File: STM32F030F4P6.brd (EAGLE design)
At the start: 19.1 x 50.8 mm, 27 parts, among them IC1 MCP170333MB, J2 455-1750-1-ND, J4 CORTEX_DEBUG_MINIMUM_PTH, U1 STM32F030F4P6

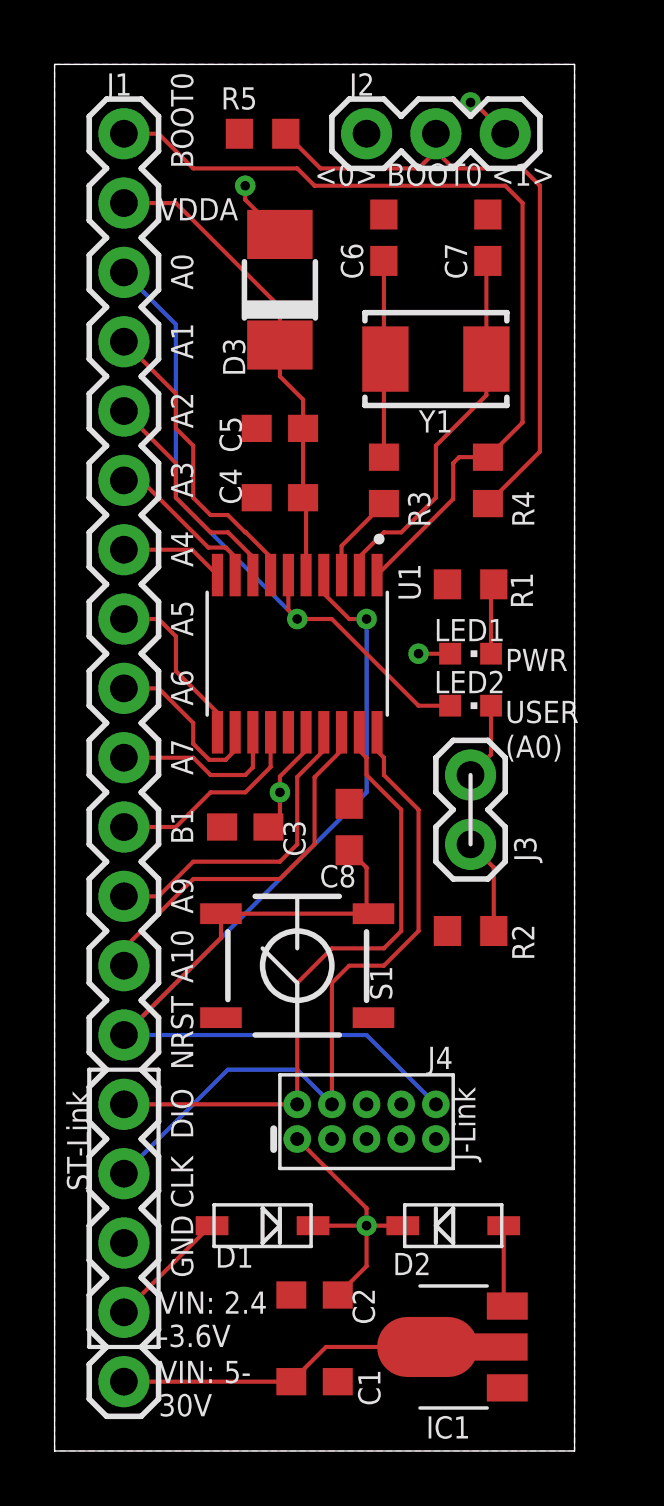
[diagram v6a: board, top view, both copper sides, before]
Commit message: Cleaned up silkcreen and checked rotation of parts on JLCPCB.
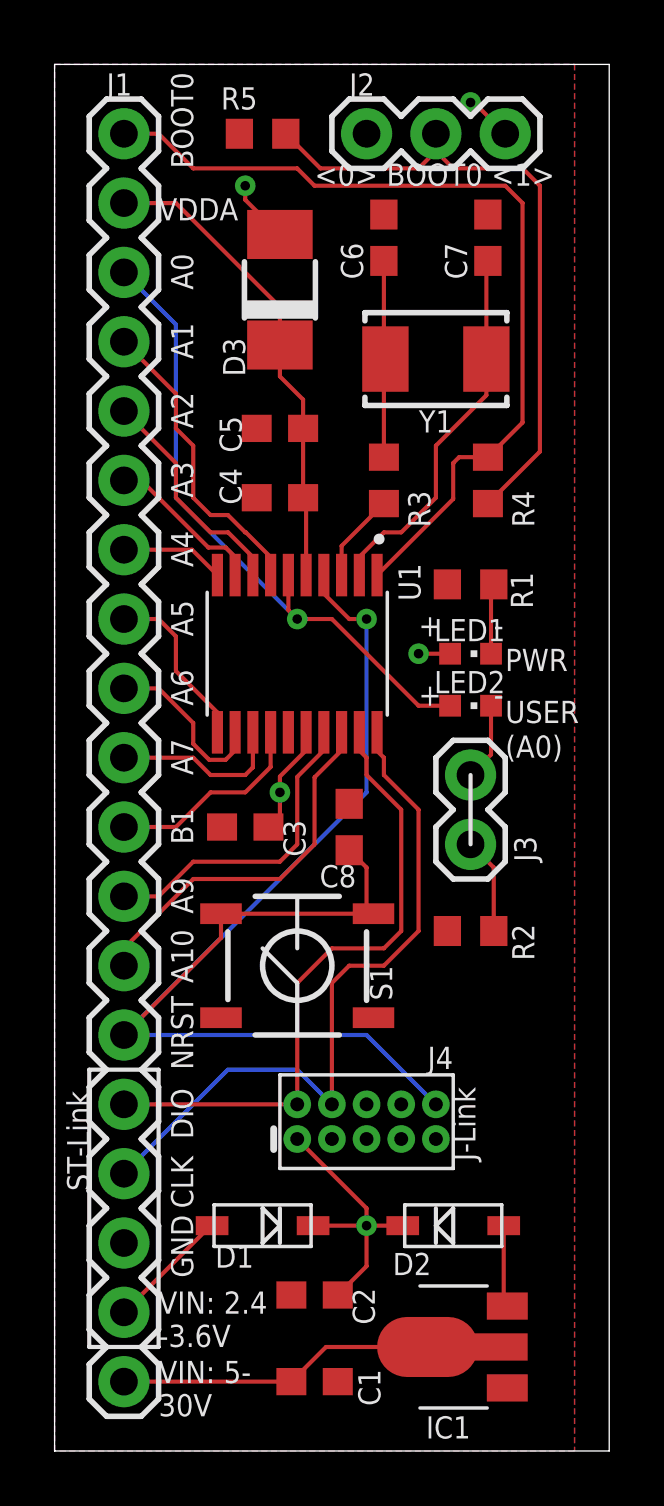
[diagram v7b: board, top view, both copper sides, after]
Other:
- board size 19.1 x 50.8 mm -> 20.3 x 50.8 mm
- board text added: "+ -"
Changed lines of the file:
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@@
 <board>
 <plain>
-<wire x1="0" y1="0" x2="19.05" y2="0" width="0" layer="20"/>
-<wire x1="19.05" y1="0" x2="19.05" y2="50.8" width="0" layer="20"/>
-<wire x1="19.05" y1="50.8" x2="0" y2="50.8" width="0" layer="20"/>
+<wire x1="0" y1="0" x2="20.32" y2="0" width="0" layer="20"/>
+<wire x1="20.32" y1="0" x2="20.32" y2="50.8" width="0" layer="20"/>
+<wire x1="20.32" y1="50.8" x2="0" y2="50.8" width="0" layer="20"/>
 <wire x1="0" y1="50.8" x2="0" y2="0" width="0" layer="20"/>
 <text x="18.415" y="46.99" size="0.8128" layer="26" rot="MR0" align="top-left">VIN, 2.4-3.6V: MCU
@@
 <wire x1="15.24" y1="24.765" x2="15.24" y2="22.225" width="0.1524" layer="21"/>
 <text x="16.51" y="25.4" size="0.8128" layer="25">(A0)</text>
+<text x="13.335" y="27.305" size="0.8128" layer="25">+      -</text>
+<text x="13.335" y="29.845" size="0.8128" layer="25">+      -</text>
 </plain>
 <attributes>
